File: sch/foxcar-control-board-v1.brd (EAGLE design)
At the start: 91.1 x 55.9 mm, 84 parts, among them J1 MICROSD, J2 XBEE-PRO, U1 SPX29300, U2 VNH5019, U3 MPU6000, U4 HMC5883LSMD, U5 STM32F4V

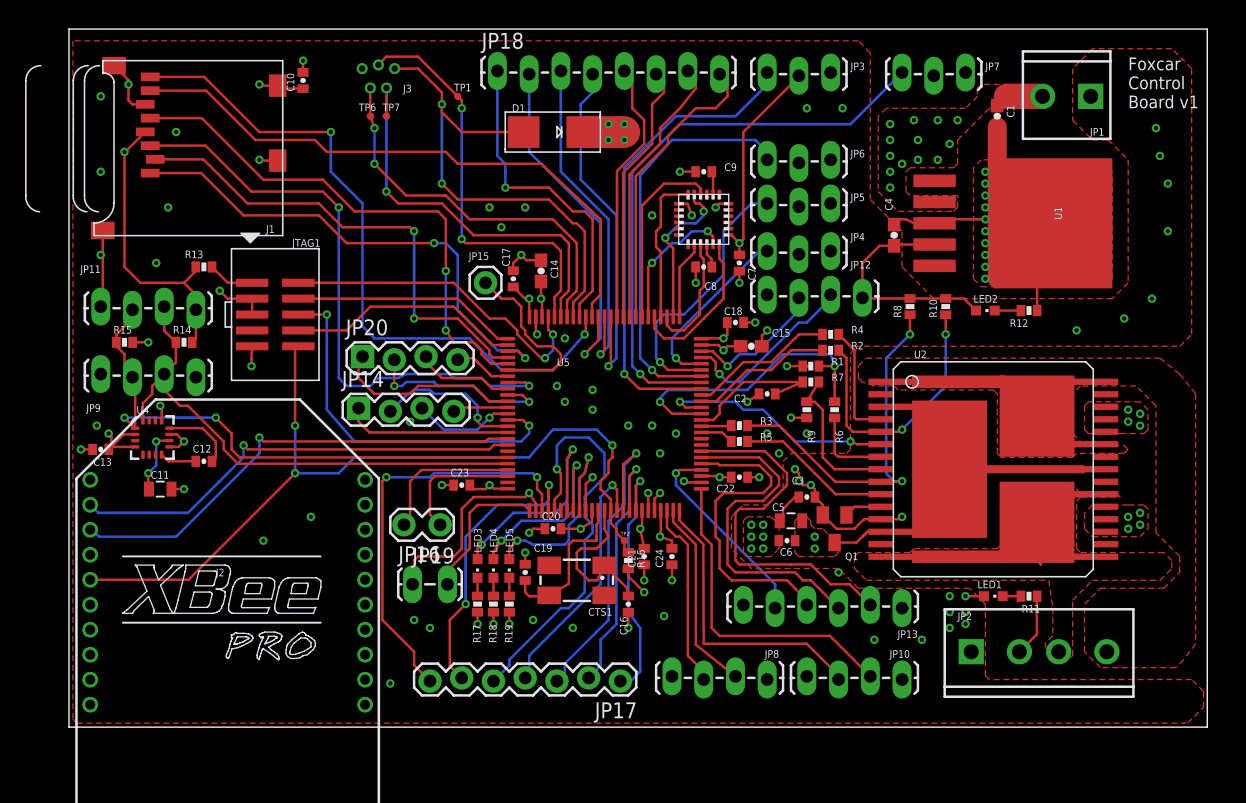
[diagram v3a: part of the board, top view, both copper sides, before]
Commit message: Added library for this repo.
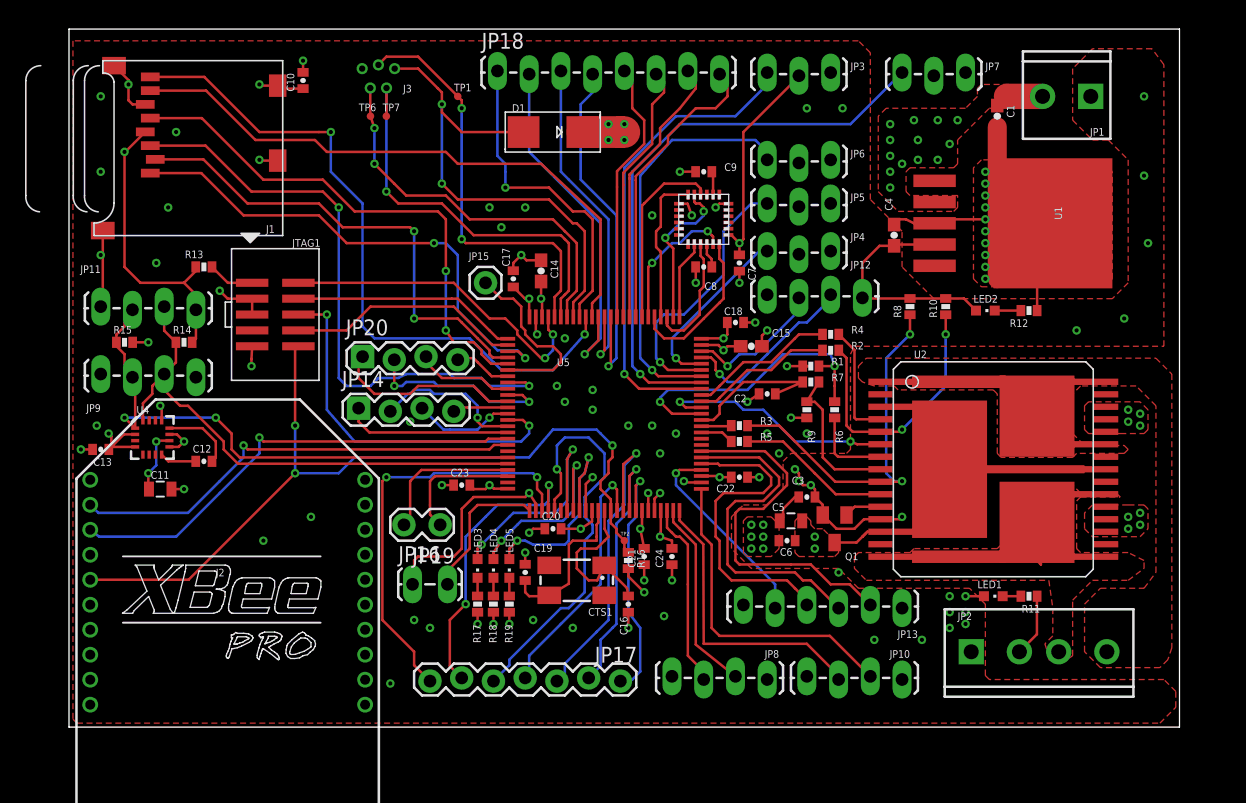
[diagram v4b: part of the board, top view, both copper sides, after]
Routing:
- net GND: vias 99 -> 97
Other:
- board size 91.1 x 55.9 mm -> 88.9 x 55.9 mm
- board text removed: "Foxcar Control Board v1"
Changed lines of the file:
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@@
 <setting verticaltext="up"/>
 </settings>
-<grid distance="1.27" unitdist="mm" unit="mm" style="dots" multiple="1" display="yes" altdistance="0.025" altunitdist="inch" altunit="inch"/>
+<grid distance="0.0125" unitdist="inch" unit="inch" style="dots" multiple="1" display="yes" altdistance="0.025" altunitdist="inch" altunit="inch"/>
 <layers>
 <layer number="1" name="Top" color="4" fill="1" visible="yes" active="yes"/>
@@
 <board>
 <plain>
-<wire x1="0" y1="0" x2="91.1025" y2="0" width="0" layer="20"/>
-<wire x1="91.1025" y1="0" x2="91.1025" y2="55.8675" width="0" layer="20"/>
-<wire x1="91.1025" y1="55.8675" x2="0" y2="55.8675" width="0" layer="20"/>
+<wire x1="0" y1="0" x2="88.88" y2="0" width="0" layer="20"/>
+<wire x1="88.88" y1="0" x2="88.88" y2="55.8675" width="0" layer="20"/>
+<wire x1="88.88" y1="55.8675" x2="0" y2="55.8675" width="0" layer="20"/>
 <wire x1="0" y1="55.8675" x2="0" y2="0" width="0" layer="20"/>
-<text x="84.7725" y="49.53" size="1.016" layer="21">Foxcar
-Control
-Board v1</text>
 </plain>
 <attributes>
@@
 <element name="JP14" library="SparkFun-Connectors" package="1X04_LOCK" value="" x="23.1775" y="25.4"/>
 <element name="JP20" library="SparkFun-Connectors" package="1X04_LOCK" value="" x="23.495" y="29.5275"/>
-<element name="JP17" library="SparkFun-Connectors" package="1X07_LOCK" value="" x="44.1325" y="3.81" rot="R180"/>
+<element name="JP17" library="SparkFun-Connectors" package="1X07_LOCK" value="" x="44.1325" y="3.81" smashed="yes" rot="R180">
+<attribute name="NAME" x="45.4787" y="6.4262" size="1.27" layer="25" ratio="10" rot="R180"/>
+<attribute name="VALUE" x="45.4025" y="6.985" size="1.27" layer="27" rot="R180"/>
+</element>
 <element name="JP19" library="SparkFun-Connectors" package="1X02_LOCK" value="" x="29.5275" y="16.1925" rot="R180"/>
 <element name="JP16" library="SparkFun-Connectors" package="1X02_LOCK_LONGPADS" value="" x="27.6225" y="11.43"/>
@@
 <vertex x="0.3175" y="0.635"/>
 <vertex x="0.635" y="0.3175"/>
-<vertex x="89.535" y="0.3175"/>
-<vertex x="90.805" y="1.5875"/>
-<vertex x="90.805" y="2.8575"/>
-<vertex x="89.8525" y="3.81"/>
+<vertex x="87.3125" y="0.3175"/>
+<vertex x="88.5825" y="1.5875"/>
+<vertex x="88.5825" y="2.8575"/>
+<vertex x="87.63" y="3.81"/>
 <vertex x="73.66" y="3.81"/>
 <vertex x="73.3425" y="4.1275"/>
@@
 <vertex x="62.5475" y="29.845"/>
 <vertex x="62.865" y="30.48"/>
-<vertex x="88.9" y="30.48"/>
-<vertex x="89.8525" y="31.4325"/>
-<vertex x="89.8525" y="52.705"/>
-<vertex x="88.265" y="54.2925"/>
+<vertex x="87.63" y="30.48"/>
+<vertex x="87.63" y="53.0225"/>
+<vertex x="86.6775" y="54.2925"/>
 <vertex x="81.915" y="54.2925"/>
 <vertex x="80.3275" y="52.705"/>
@@
 <via x="80.645" y="31.75" extent="1-16" drill="0.3302" diameter="0.6858"/>
 <via x="84.455" y="32.7025" extent="1-16" drill="0.3302" diameter="0.6858"/>
-<via x="86.6775" y="34.29" extent="1-16" drill="0.3302" diameter="0.6858"/>
-<via x="87.9475" y="39.6875" extent="1-16" drill="0.3302" diameter="0.6858"/>
-<via x="87.9475" y="43.4975" extent="1-16" drill="0.3302" diameter="0.6858"/>
-<via x="87.3125" y="45.72" extent="1-16" drill="0.3302" diameter="0.6858"/>
-<via x="86.995" y="47.9425" extent="1-16" drill="0.3302" diameter="0.6858"/>
+<via x="86.36" y="38.735" extent="1-16" drill="0.3302" diameter="0.6858"/>
+<via x="86.0425" y="44.1325" extent="1-16" drill="0.3302" diameter="0.6858"/>
+<via x="86.0425" y="50.4825" extent="1-16" drill="0.3302" diameter="0.6858"/>
 <via x="59.055" y="49.53" extent="1-16" drill="0.3302" diameter="0.6858"/>
 <via x="61.9125" y="49.53" extent="1-16" drill="0.3302" diameter="0.6858"/>
@@
 <vertex x="80.3275" y="10.16"/>
 <vertex x="81.915" y="11.7475"/>
-<vertex x="87.3125" y="11.7475"/>
-<vertex x="88.265" y="12.7"/>
-<vertex x="88.265" y="13.335"/>
-<vertex x="87.63" y="13.97"/>
+<vertex x="84.7725" y="11.7475"/>
+<vertex x="86.0425" y="12.7"/>
+<vertex x="86.0425" y="13.335"/>
+<vertex x="84.7725" y="13.97"/>
 <vertex x="80.9625" y="13.97"/>
 <vertex x="80.645" y="14.2875"/>
@@
 <vertex x="63.1825" y="28.8925"/>
 <vertex x="63.8175" y="29.5275"/>
-<vertex x="87.3125" y="29.5275"/>
-<vertex x="88.9" y="28.2575"/>
-<vertex x="90.17" y="26.67"/>
-<vertex x="90.17" y="6.6675"/>
-<vertex x="89.2175" y="5.3975"/>
-<vertex x="88.5825" y="4.7625"/>
+<vertex x="86.995" y="29.5275"/>
+<vertex x="88.265" y="28.2575"/>
+<vertex x="88.265" y="6.35"/>
+<vertex x="87.9475" y="5.3975"/>
+<vertex x="87.3125" y="4.7625"/>
 <vertex x="82.55" y="4.7625"/>
 <vertex x="81.28" y="6.0325"/>
 <vertex x="81.28" y="9.8425"/>
 <vertex x="82.55" y="11.1125"/>
-<vertex x="87.63" y="11.1125"/>
-<vertex x="88.9" y="12.3825"/>
-<vertex x="88.9" y="13.6525"/>
-<vertex x="86.995" y="15.5575"/>
+<vertex x="86.0425" y="11.1125"/>
+<vertex x="86.995" y="12.3825"/>
 <vertex x="86.995" y="25.7175"/>
 <vertex x="85.4075" y="27.305"/>
@@
 </board>
 </drawing>
-<compatibility>
-<note version="6.3" minversion="6.2.2" severity="warning">
-Since Version 6.2.2 text objects can contain more than one line,
-which will not be processed correctly with this version.
-</note>
-</compatibility>
 </eagle>

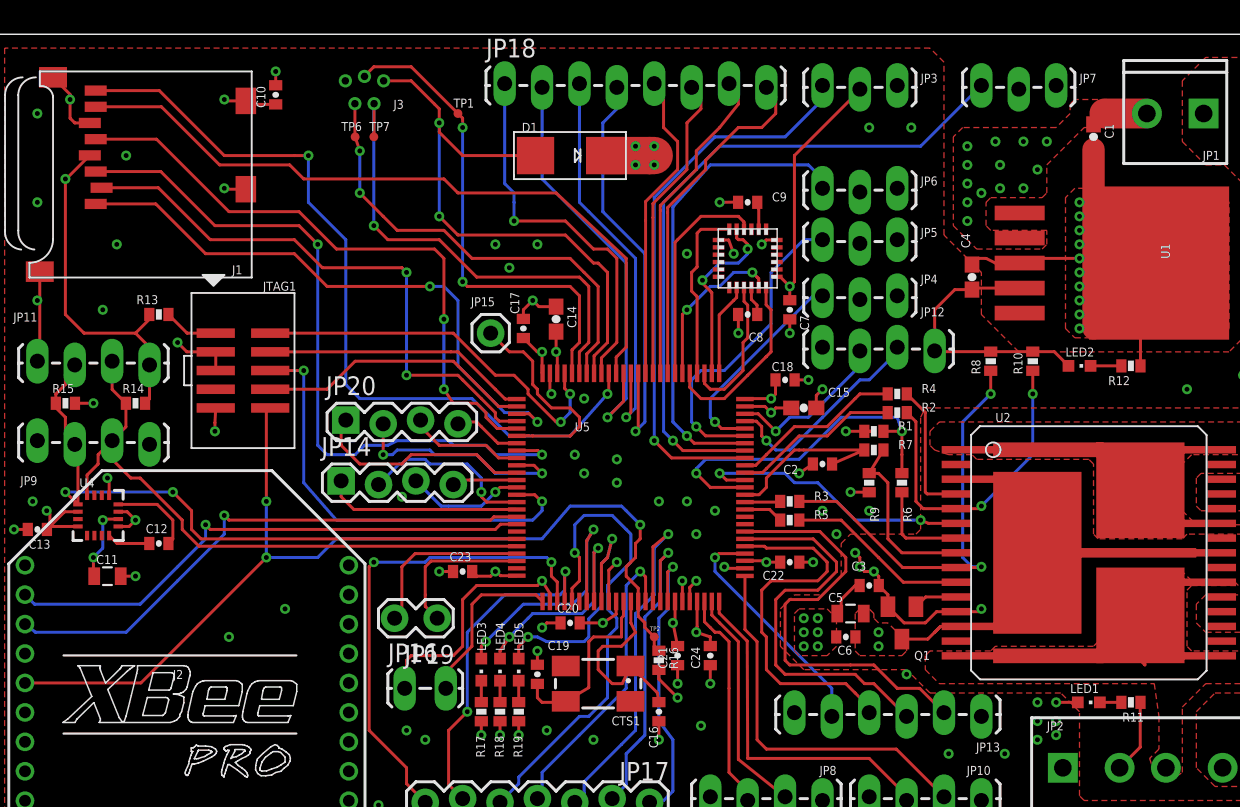
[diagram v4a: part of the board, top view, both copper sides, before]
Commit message: Made BOM and had to make some changes. Final parts list included.
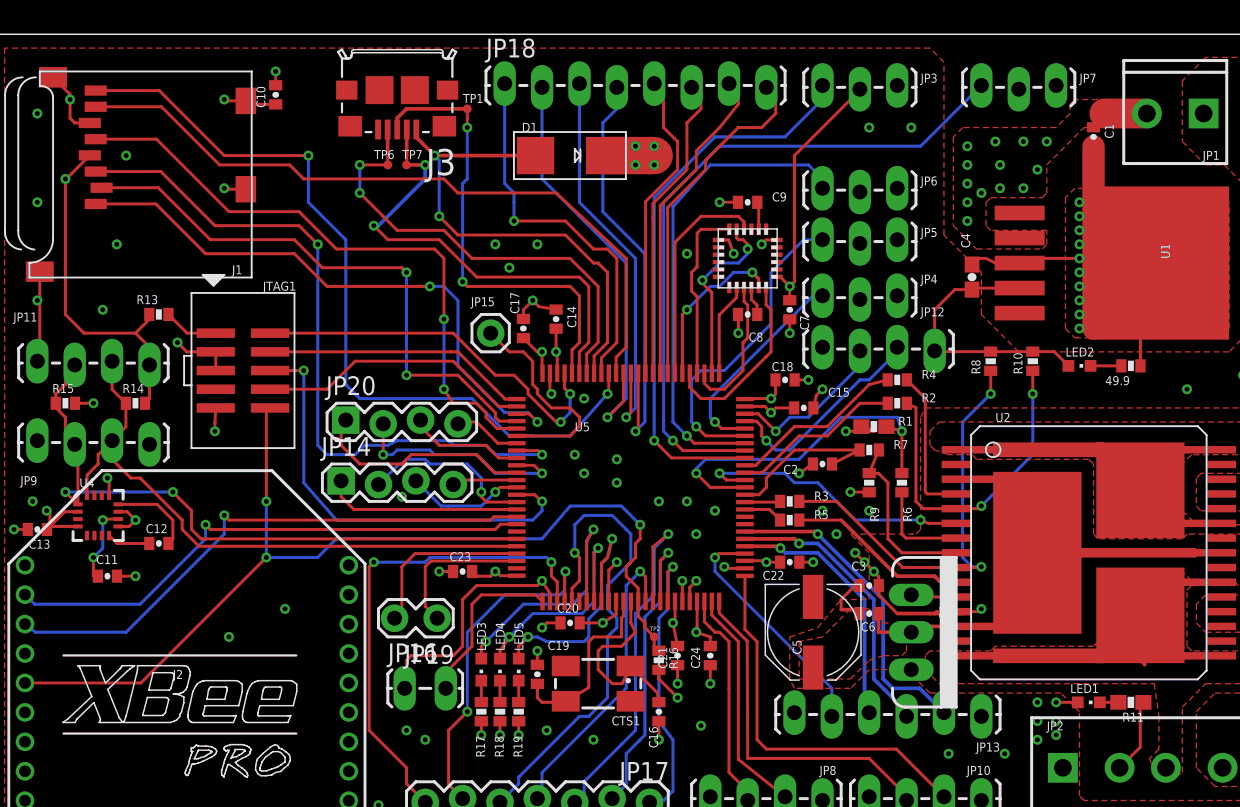
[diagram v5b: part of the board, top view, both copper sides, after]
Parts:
- C1, C14, C15: device SparkFun-Passives:0603-CAP -> SparkFun-Passives:0402-CAP
- C11: device SparkFun-Passives:0805 -> SparkFun-Passives:0402-CAP
- C16, C19: value 16pF -> 15pF
- C5: device SparkFun-Passives:0805 -> SparkFun-Passives:PANASONIC_D
- J3: device SparkFun:MICRO-B-RA-TH -> dp_devices:CONN_USB_MICRO-B
- Q1: value (none) -> N-MOSFET; device adafruit:SOT23 -> SparkFun-DiscreteSemi:TO220V
- R1, R11: device SparkFun-Passives:0402-RES -> SparkFun-Passives:0603-RES
- R17, R18, R19: value 50 -> 49.9
- moved TP6 2.93 mm to (26.4, 47.0)
- moved TP7 2.93 mm to (27.6, 47.0)
- moved C5 2.84 mm to (55.2, 15.2), turned to 270 degrees
- moved C6 2.25 mm to (59.1, 16.5)
- moved J3 2.25 mm to (27.0, 52.1)
- moved R4 0.95 mm to (61.0, 32.4)
- moved Q1 0.90 mm to (61.9, 15.2), turned to 270 degrees
- moved TP1 0.71 mm to (31.8, 50.8)
- moved R2 0.63 mm to (61.0, 30.8)
- moved R1 0.32 mm to (59.4, 29.2)
- moved R7 0.32 mm to (59.1, 27.6)
- renumbered R12 to 49.9
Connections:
- net FS_DM: now also J3.P2; no longer J3.2
- net FS_DP: now also J3.P3; no longer J3.3
- net FS_ID: now also J3.P4; no longer J3.4
- net FS_VBUS: now also J3.P1; no longer J3.1
- net GND: now also C5.-, J3.P5; no longer C5.2, J3.5
- net VCC: now also C5.+, Q1.2; no longer C5.1, Q1.3
- net VIN: now also Q1.3; no longer Q1.2
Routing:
- net SPI1_SCK: track 25.6 -> 17.4 mm, vias 0 -> 1
- net SPI1_MISO: track 27.2 -> 19.3 mm, vias 0 -> 1
- net SPI1_MOSI: track 29.7 -> 21.8 mm, vias 0 -> 1
- net FS_VBUS: track 39.9 -> 34.1 mm
- net VCC: track 5.51 -> 7.67 mm, vias 2 -> 0
- net GND: track 100.2 -> 102.1 mm, vias 97 -> 90
- net FS_DP: track 33.3 -> 31.5 mm
- net FS_DM: track 33.0 -> 31.9 mm, vias 1 -> 2
- net VIN: track 21.7 -> 22.7 mm
- net INA: track 9.35 -> 10.3 mm
- net ENA: track 21.6 -> 22.4 mm
- net MD_CS: track 12.1 -> 11.5 mm

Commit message: Ready for control board build.
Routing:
- net FS_DM: track 31.9 -> 27.2 mm
- net GND: vias 90 -> 89
